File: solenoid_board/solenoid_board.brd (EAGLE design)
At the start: 39.4 x 38.1 mm, 28 parts, among them Q1 MOSFET-NCHANNELSMD, Q2 MOSFET-NCHANNELSMD, Q3 MOSFET-NCHANNELSMD, Q4 MOSFET-NCHANNELSMD

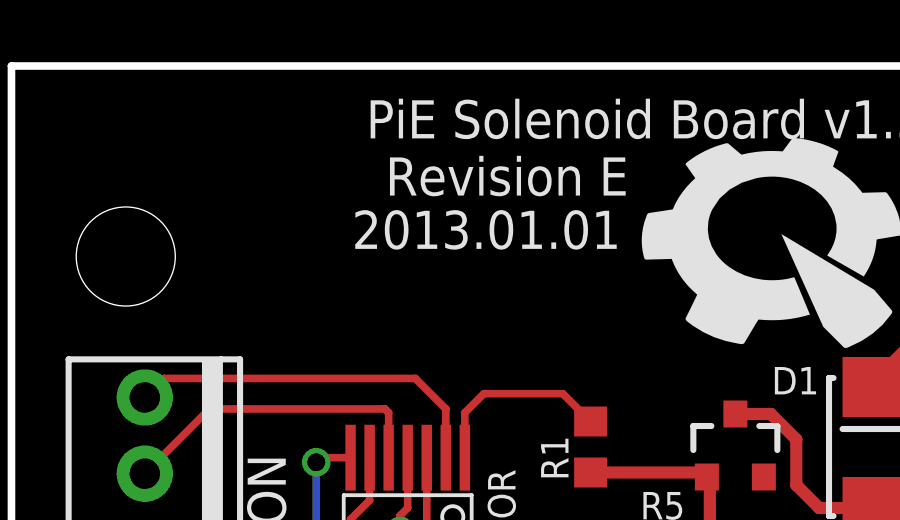
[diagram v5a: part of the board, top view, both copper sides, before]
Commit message: Sherlock, Watson, Solenoid Rev F
- Removed 5V pin from Servo on Watson
- Removed Low Battery LED on Sherlock
- Added copyright info to all boards
- Put OSHW logos in pie.lbr

Sherlock DFM: https://www.freedfm.com/freedfm/0019486703437089/results/summary2.htm
Watson DFM: https://www.freedfm.com/freedfm/0019486703437092/results/summary2.htm
Solenoid DFM: https://www.freedfm.com/freedfm/0019486703437091/results/summary2.htm

Change-Id: I06acc4df022cd5501e47e2ba488eae3a4c23d9a5
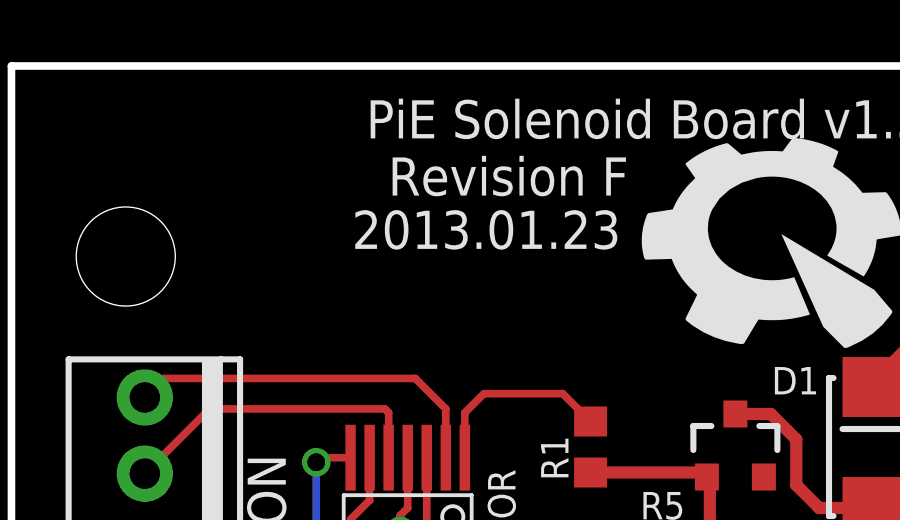
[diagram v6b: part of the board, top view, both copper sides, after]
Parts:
- added U$5: (no value), pie:OSHW-LOGO-M
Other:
- board text added: "2013.01.23"
- board text added: "Copyright (c) 2013, Pioneers in Engineering All rights reserved. Design by: Sumita Ghosh, and Sahar Mesri This design is open source hardware. For more information, visit pioneers.berkeley.edu/ opensource"
- board text added: "Revision F"
- board text removed: "2013.01.01"
- board text removed: "Revision E"
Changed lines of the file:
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@@
 <wire x1="0" y1="38.1" x2="0" y2="0" width="0.254" layer="20"/>
 <text x="30.48" y="36.957" size="1.27" layer="25" font="vector" ratio="20" rot="R180">PiE Solenoid Board v1.5</text>
-<text x="20.574" y="35.052" size="1.27" layer="21" font="vector" ratio="20" rot="R180">Revision E</text>
-<text x="20.32" y="33.274" size="1.27" layer="21" font="vector" ratio="20" rot="R180">2013.01.01</text>
+<text x="20.574" y="35.052" size="1.27" layer="21" font="vector" ratio="20" rot="R180">Revision F</text>
+<text x="20.32" y="33.274" size="1.27" layer="21" font="vector" ratio="20" rot="R180">2013.01.23</text>
 <text x="2.032" y="10.16" size="1.27" layer="21" font="vector" ratio="20">POWER</text>
 <text x="9.144" y="15.494" size="1.27" layer="21" font="vector" ratio="20" rot="SR90">TO WATSON</text>
+<text x="33.528" y="15.113" size="1.27" layer="22" font="vector" ratio="15" rot="MR0">Copyright (c) 2013,
+Pioneers in Engineering
+All rights reserved.
+Design by: Sumita Ghosh,
+and Sahar Mesri
+This design is open
+source hardware.
+For more information,
+visit
+pioneers.berkeley.edu/
+opensource</text>
 </plain>
 <attributes>
@@
 </class>
 </classes>
-<designrules name="advancedcircuits-33each-pieNEW">
+<designrules name="advancedcircuits-33each-pie">
 <description language="de">&lt;b&gt;EAGLE Design Rules&lt;/b&gt;
 &lt;p&gt;
@@
 <element name="U$3" library="pie" package="STAND-OFF" value="Mounting + Test" x="3.81" y="31.75"/>
 <element name="U$4" library="pie" package="STAND-OFF" value="Mounting + Test" x="35.56" y="6.35"/>
+<element name="U$5" library="pie" package="OSHW-LOGO-M" value="" x="15.24" y="13.589" rot="MR0"/>
 </elements>
 <signals>
@@
 </board>
 </drawing>
+<compatibility>
+<note version="6.3" minversion="6.2.2" severity="warning">
+Since Version 6.2.2 text objects can contain more than one line,
+which will not be processed correctly with this version.
+</note>
+</compatibility>
 </eagle>
